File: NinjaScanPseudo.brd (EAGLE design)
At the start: 25.4 x 35.6 mm, 57 parts, among them CON2 ZX62-B-5PA(11), CON3 JST_SH-12SM, IC1 LTC3550EDHC, IC2 MPU-6000, IC4 MAG3110FCR, J1 JUMPER1608, U1 DM3AT-SF-PEJM5, U2 H.FL, U3 NEO-6T, U4 MS5611-01BA01

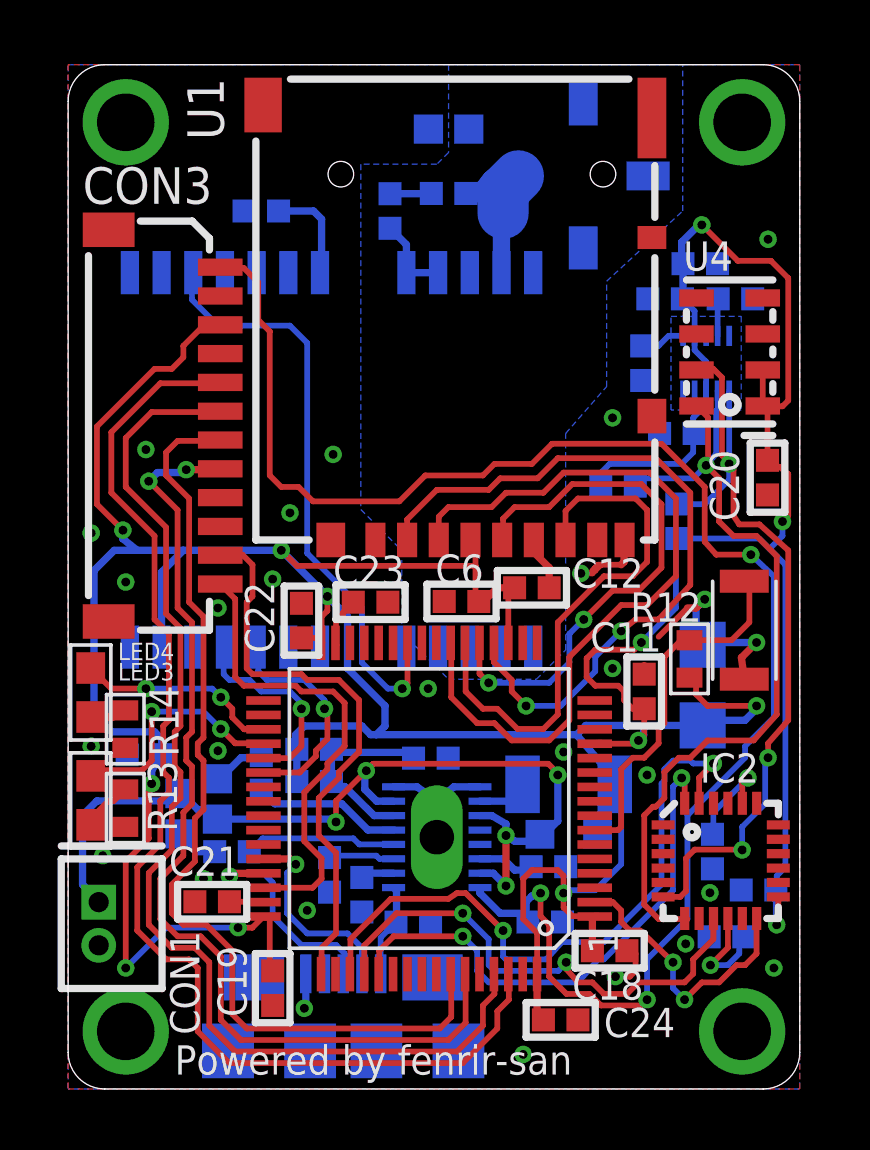
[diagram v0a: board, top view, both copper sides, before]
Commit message: XTAL added
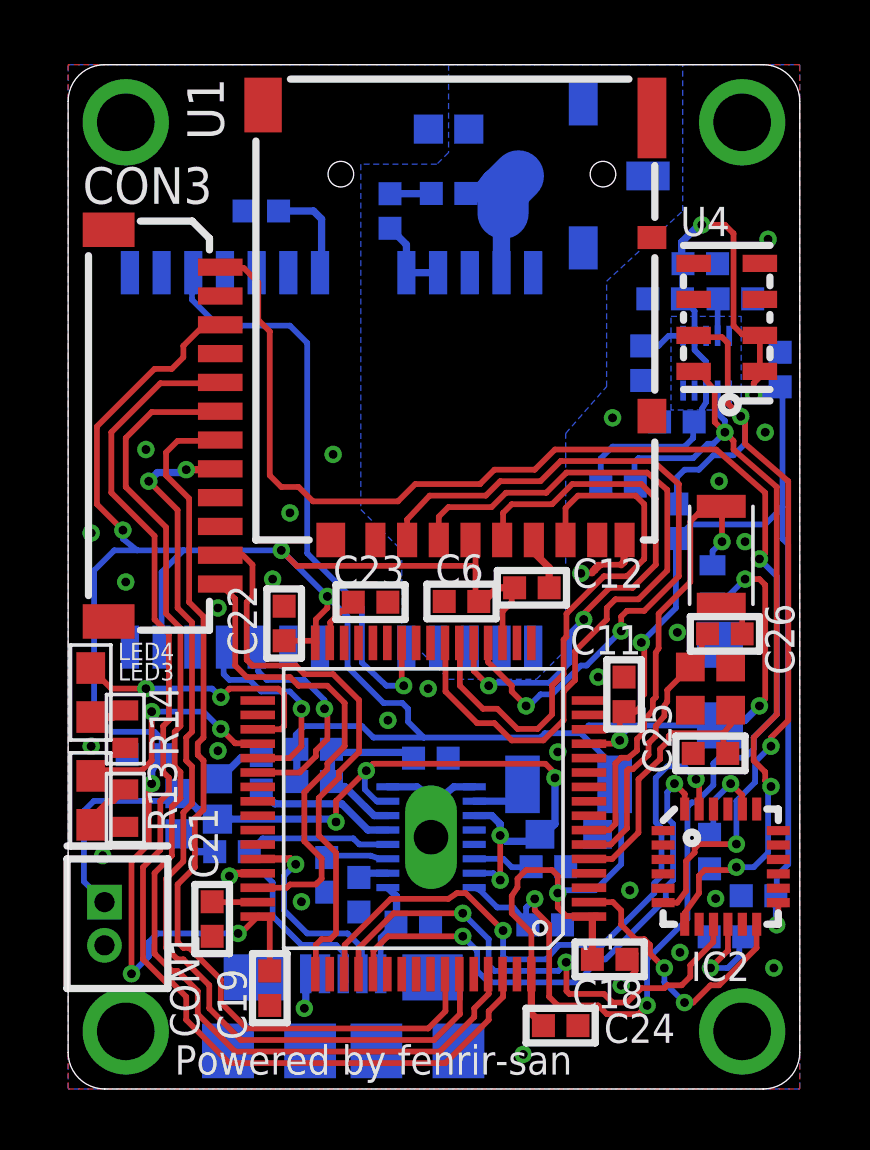
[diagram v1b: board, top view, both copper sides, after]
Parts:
- added C25, C26: 12pF, additional:1005
- added U$15: FA128, mami_pero:FA128
- moved C20 3.78 mm to (24.7, 25.0), flipped to the bottom, turned to 270 degrees
- moved U$8 2.72 mm to (22.7, 16.8)
- moved R12 2.72 mm to (22.4, 18.2), flipped to the bottom
- moved U4 1.20 mm to (22.9, 26.8)
- moved C11 0.71 mm to (19.3, 13.7)
- moved C22 0.61 mm to (7.50, 16.2)
- moved C1 0.60 mm to (22.6, 14.0)
- moved C21 0.60 mm to (5.00, 5.90), turned to 90 degrees
- moved C17 0.40 mm to (21.1, 23.2)
- moved C18 0.30 mm to (18.8, 4.50)
- moved IC1 0.20 mm to (12.6, 8.74)
- moved C9 0.20 mm to (24.0, 6.71)
- moved IC2 0.20 mm to (22.7, 7.72)
- moved CON1 0.20 mm to (1.26, 5.74)
- moved C24 0.20 mm to (17.1, 2.20)
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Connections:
- new net XTAL_IN: C25.P$2, U$15.1, U$6.P$5
- new net XTAL_OUT: C26.P$2, U$15.3, U$6.P$6
- net GND: now also C25.P$1, C26.P$1
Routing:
- net XTAL_OUT: track 0.00 -> 9.65 mm
- net XTAL_IN: track 0.00 -> 9.56 mm
- net GND: track 20.2 -> 14.3 mm, vias 31 -> 33
- net +3V: track 168.5 -> 174.0 mm, vias 13 -> 14
- net N$21: track 13.7 -> 16.6 mm, vias 0 -> 1
- net N$4: track 7.05 -> 9.88 mm
- net VCC: track 57.5 -> 59.1 mm
- net SMB0_SDA: track 28.8 -> 30.3 mm
- net USART1_RX: track 34.8 -> 33.9 mm
- net USART1_TX: track 33.5 -> 32.7 mm
- net I2C1_SCL: track 40.3 -> 39.5 mm
- net I2C1_SDA: track 41.5 -> 40.7 mm
- net SPI1_CS: track 25.5 -> 24.7 mm
- net N$31: track 1.37 -> 2.16 mm
- net IMU_MISO: track 17.5 -> 18.1 mm
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
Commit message: CMOS Xtal added
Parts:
- removed C25: 12pF, additional:1005
- C26: value 12pF -> 0.01u
- U$15: value FA128 -> SG-210; device mami_pero:FA128 -> mami_pero:EPSON_2.5X2.0X0.8MM
- moved C26 3.54 mm to (22.3, 12.3), turned to 0 degrees
- moved U$15 1.75 mm to (23.0, 15.0), turned to 180 degrees
- moved C6 0.20 mm to (13.5, 16.9)
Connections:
- removed net XTAL_OUT: C26.P$2, U$15.3, U$6.P$6
- net +3V: now also C26.P$2, U$15.P$1, U$15.P$4
- net GND: now also U$15.P$2; no longer C25.P$1
- net XTAL_IN: now also U$15.P$3; no longer C25.P$2, U$15.1
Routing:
- net XTAL_OUT: track 9.65 -> 0.00 mm
- net +3V: track 174.0 -> 178.2 mm
- net GND: track 14.3 -> 16.9 mm
- net XTAL_IN: track 9.56 -> 7.55 mm
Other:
- board text added: "Lysenko"
- board text added: "Rev. A"

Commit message: Final update of Rev.A
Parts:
- moved R14 0.16 mm to (2.14, 11.8)
- moved C22 0.15 mm to (7.35, 16.2)
- moved LED2 0.15 mm to (4.03, 9.56)
- moved R13 0.15 mm to (2.13, 9.10)
- moved C23 0.11 mm to (10.6, 17.0)
- moved LED1 0.10 mm to (5.28, 10.1)
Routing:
- net N$20: track 8.77 -> 10.6 mm
- net GPS_TX: track 7.26 -> 8.53 mm
- net GPS_RX: track 8.05 -> 9.13 mm
- net I2C1_SCL: track 39.5 -> 40.2 mm
- net USART1_TX: track 32.7 -> 33.4 mm
- net I2C1_SDA: track 40.7 -> 41.4 mm
- net USART1_RX: track 33.9 -> 34.6 mm
- net SWDIO: track 16.7 -> 17.3 mm
- net N$19: track 32.7 -> 33.3 mm
